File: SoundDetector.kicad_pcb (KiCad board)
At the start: 2 copper layers, 50.8 x 22.9 mm, 6 parts, among them J1 feather long, J2 feather short

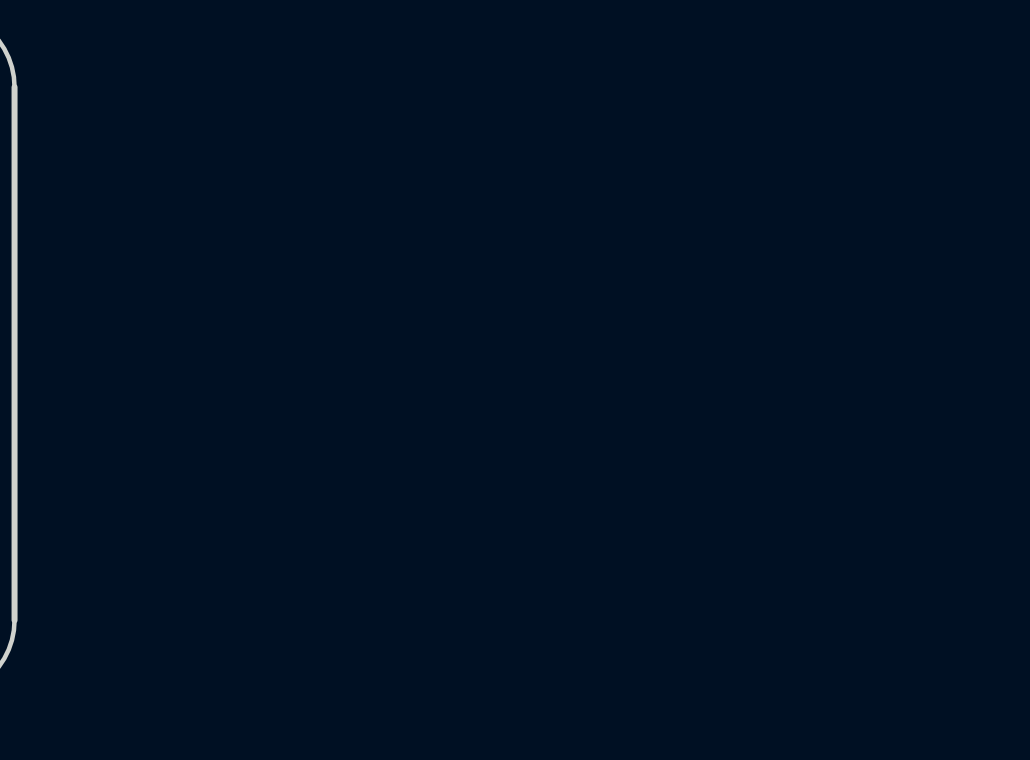
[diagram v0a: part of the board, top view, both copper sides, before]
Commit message: Import new footprints into PCB.
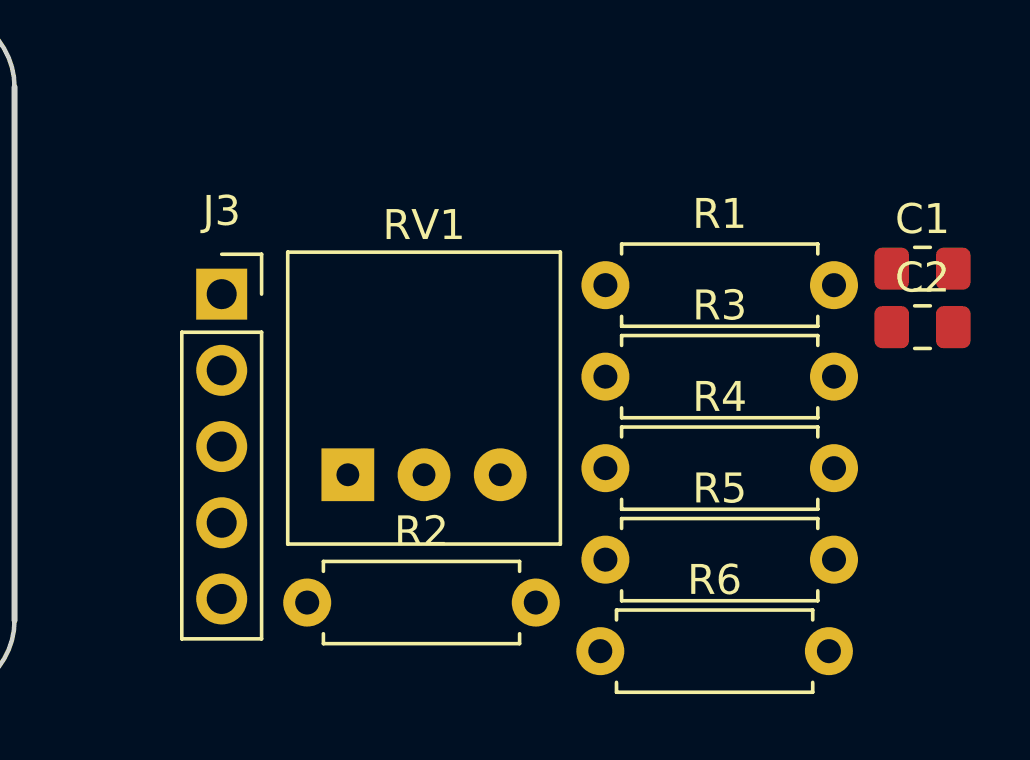
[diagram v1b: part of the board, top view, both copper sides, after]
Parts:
- added C1: 10μF, Capacitor_SMD:C_0805_2012Metric_Pad1.15x1.40mm_HandSolder, F.Cu at (106.5, 34.0)
- added C2: 10μF, Capacitor_SMD:C_0805_2012Metric_Pad1.15x1.40mm_HandSolder, F.Cu at (106.5, 35.9)
- added J3: sound detector, Connector_PinSocket_2.54mm:PinSocket_1x05_P2.54mm_Vertical, F.Cu at (83.1, 34.8)
- added R1: 1.74K, Resistor_THT:R_Axial_DIN0207_L6.3mm_D2.5mm_P7.62mm_Horizontal, F.Cu at (95.9, 34.5)
- added R2: 3.3K, Resistor_THT:R_Axial_DIN0207_L6.3mm_D2.5mm_P7.62mm_Horizontal, F.Cu at (86.0, 45.1)
- added R3: 1.74K, Resistor_THT:R_Axial_DIN0207_L6.3mm_D2.5mm_P7.62mm_Horizontal, F.Cu at (95.9, 37.6)
- added R4: 3.3K, Resistor_THT:R_Axial_DIN0207_L6.3mm_D2.5mm_P7.62mm_Horizontal, F.Cu at (95.9, 40.6)
- added R5: 1.74K, Resistor_THT:R_Axial_DIN0207_L6.3mm_D2.5mm_P7.62mm_Horizontal, F.Cu at (95.9, 43.7)
- added R6: 3.3K, Resistor_THT:R_Axial_DIN0207_L6.3mm_D2.5mm_P7.62mm_Horizontal, F.Cu at (95.7, 46.7)
- added RV1: 10K, footprints:Potentiometer_Bourns_3352T_Vertical, F.Cu at (87.3, 40.9)

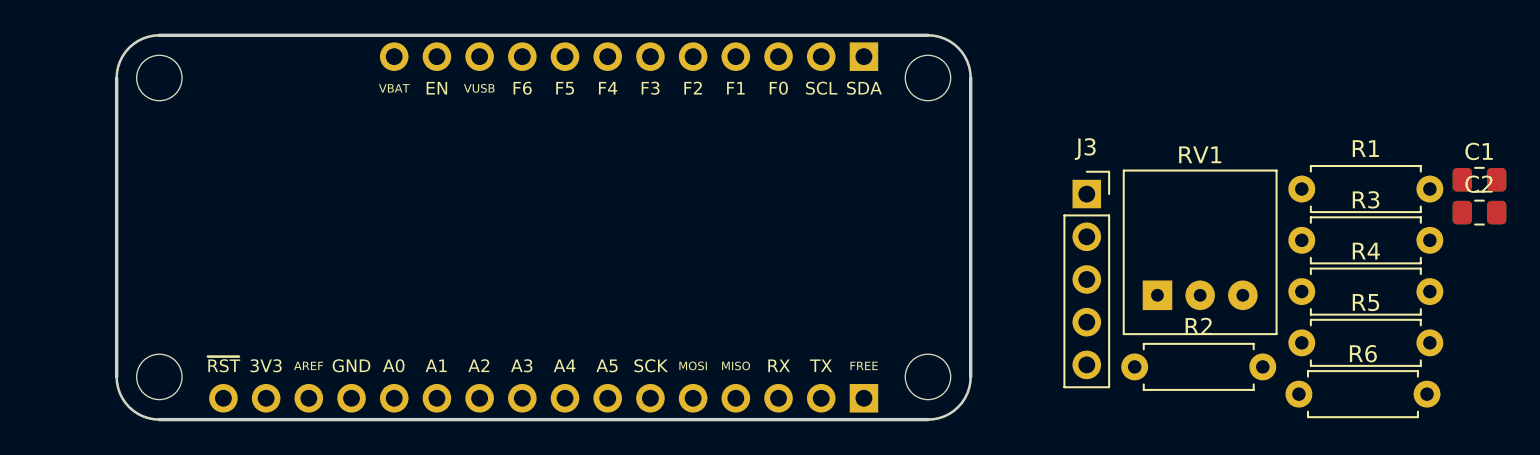
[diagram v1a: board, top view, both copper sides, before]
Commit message: Position footprints on PCB.
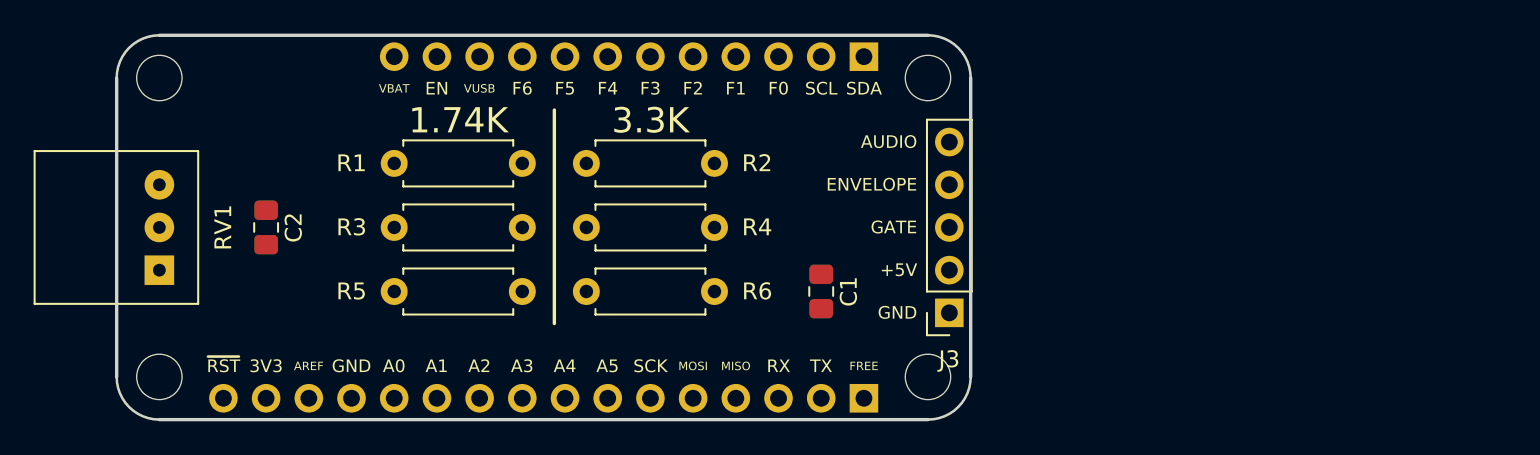
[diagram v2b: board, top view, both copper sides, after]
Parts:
- moved C2 72.2 mm to (34.3, 36.8), turned to 270 degrees
- moved RV1 59.4 mm to (27.9, 39.4), turned to 90 degrees
- moved R5 54.1 mm to (41.9, 40.6)
- moved R1 54.0 mm to (41.9, 33.0)
- moved R3 54.0 mm to (41.9, 36.8)
- moved R6 42.8 mm to (53.3, 40.6)
- moved R4 42.7 mm to (53.3, 36.8)
- moved C1 39.7 mm to (67.3, 40.6), turned to 270 degrees
- moved R2 34.8 mm to (53.3, 33.0)
- moved J3 10.8 mm to (74.9, 41.9), turned to 180 degrees
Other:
- board text added: "+5V"
- board text added: "1.74K"
- board text added: "3.3K"
- board text added: "AUDIO"
- board text added: "ENVELOPE"
- board text added: "GATE"

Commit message: Draw all the tracks.
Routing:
- net /VUSB: track 0.00 -> 41.2 mm, vias 0 -> 1
- net /GATE: track 0.00 -> 34.6 mm
- net /ENV: track 0.00 -> 34.1 mm
- net /AUD: track 0.00 -> 33.5 mm
- net /A2: track 0.00 -> 31.4 mm, vias 0 -> 1
- net /F0: track 0.00 -> 31.0 mm, vias 0 -> 1
- net /A0: track 0.00 -> 23.9 mm, vias 0 -> 1
- net +3V3: track 0.00 -> 21.2 mm, vias 0 -> 1
- net /A1: track 0.00 -> 19.1 mm, vias 0 -> 1
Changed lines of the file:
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@@
     (thickness 1.6)
     (drawings 44)
-    (tracks 0)
+    (tracks 48)
     (zones 0)
     (modules 16)
@@
   (setup
     (last_trace_width 0.25)
+    (user_trace_width 0.508)
     (trace_clearance 0.2)
     (zone_clearance 0.508)
@@
   (gr_line (start 76.2 27.94) (end 76.2 45.72) (layer Edge.Cuts) (width 0.2))
   (gr_line (start 27.94 25.4) (end 73.66 25.4) (layer Edge.Cuts) (width 0.2))
+  (segment (start 43.724999 36.680003) (end 43.724999 36.285001) (width 0.25) (layer F.Cu) (net 10))
+  (segment (start 27.94 36.83) (end 34.85319 36.83) (width 0.25) (layer F.Cu) (net 10))
+  (segment (start 34.85319 36.83) (end 35.978191 37.955001) (width 0.25) (layer F.Cu) (net 10))
+  (segment (start 35.978191 37.955001) (end 42.450001 37.955001) (width 0.25) (layer F.Cu) (net 10))
+  (segment (start 42.450001 37.955001) (end 43.724999 36.680003) (width 0.25) (layer F.Cu) (net 10))
+  (via (at 45.72 35.56) (size 0.8) (drill 0.4) (layers F.Cu B.Cu) (net 10))
+  (segment (start 44.45 35.56) (end 45.72 35.56) (width 0.25) (layer F.Cu) (net 10))
+  (segment (start 43.724999 36.285001) (end 44.45 35.56) (width 0.25) (layer F.Cu) (net 10))
+  (segment (start 45.72 45.72) (end 46.99 46.99) (width 0.25) (layer B.Cu) (net 10))
+  (segment (start 45.72 35.56) (end 45.72 45.72) (width 0.25) (layer B.Cu) (net 10))
+  (segment (start 49.53 36.83) (end 53.34 36.83) (width 0.25) (layer F.Cu) (net 11))
+  (via (at 44.45 36.83) (size 0.8) (drill 0.4) (layers F.Cu B.Cu) (net 11))
+  (segment (start 49.53 36.83) (end 44.45 36.83) (width 0.25) (layer F.Cu) (net 11))
+  (segment (start 44.45 36.83) (end 44.45 46.99) (width 0.25) (layer B.Cu) (net 11))
+  (segment (start 49.53 33.02) (end 53.34 33.02) (width 0.25) (layer F.Cu) (net 12))
+  (via (at 44.45 33.02) (size 0.8) (drill 0.4) (layers F.Cu B.Cu) (net 12))
+  (segment (start 49.53 33.02) (end 44.45 33.02) (width 0.25) (layer F.Cu) (net 12))
+  (segment (start 42.759999 46.140001) (end 41.91 46.99) (width 0.25) (layer B.Cu) (net 12))
+  (segment (start 43.18 45.72) (end 42.759999 46.140001) (width 0.25) (layer B.Cu) (net 12))
+  (segment (start 43.18 34.29) (end 43.18 45.72) (width 0.25) (layer B.Cu) (net 12))
+  (segment (start 44.45 33.02) (end 43.18 34.29) (width 0.25) (layer B.Cu) (net 12))
+  (segment (start 32.775 34.29) (end 34.29 35.805) (width 0.508) (layer F.Cu) (net 15))
+  (segment (start 27.94 34.29) (end 32.775 34.29) (width 0.508) (layer F.Cu) (net 15))
+  (via (at 36.83 36.83) (size 0.8) (drill 0.4) (layers F.Cu B.Cu) (net 15))
+  (segment (start 35.805 35.805) (end 36.83 36.83) (width 0.508) (layer F.Cu) (net 15))
+  (segment (start 34.29 35.805) (end 35.805 35.805) (width 0.508) (layer F.Cu) (net 15))
+  (segment (start 34.29 39.37) (end 34.29 46.99) (width 0.508) (layer B.Cu) (net 15))
+  (segment (start 36.83 36.83) (end 34.29 39.37) (width 0.508) (layer B.Cu) (net 15))
+  (segment (start 49.53 40.64) (end 53.34 40.64) (width 0.25) (layer F.Cu) (net 19))
+  (via (at 64.77 41.91) (size 0.8) (drill 0.4) (layers F.Cu B.Cu) (net 19))
+  (segment (start 54.61 41.91) (end 64.77 41.91) (width 0.25) (layer F.Cu) (net 19))
+  (segment (start 53.34 40.64) (end 54.61 41.91) (width 0.25) (layer F.Cu) (net 19))
+  (segment (start 64.77 41.91) (end 64.77 26.67) (width 0.25) (layer B.Cu) (net 19))
+  (segment (start 67.555 39.37) (end 67.31 39.615) (width 0.508) (layer F.Cu) (net 26))
+  (segment (start 74.93 39.37) (end 67.555 39.37) (width 0.508) (layer F.Cu) (net 26))
+  (via (at 46.99 39.37) (size 0.8) (drill 0.4) (layers F.Cu B.Cu) (net 26))
+  (segment (start 47.368372 38.991628) (end 46.99 39.37) (width 0.508) (layer F.Cu) (net 26))
+  (segment (start 66.686628 38.991628) (end 47.368372 38.991628) (width 0.508) (layer F.Cu) (net 26))
+  (segment (start 67.31 39.615) (end 66.686628 38.991628) (width 0.508) (layer F.Cu) (net 26))
+  (segment (start 46.99 39.37) (end 46.99 26.67) (width 0.508) (layer B.Cu) (net 26))
+  (segment (start 44.594999 37.955001) (end 42.709999 39.840001) (width 0.25) (layer F.Cu) (net 29))
+  (segment (start 73.804999 37.955001) (end 44.594999 37.955001) (width 0.25) (layer F.Cu) (net 29))
+  (segment (start 42.709999 39.840001) (end 41.91 40.64) (width 0.25) (layer F.Cu) (net 29))
+  (segment (start 74.93 36.83) (end 73.804999 37.955001) (width 0.25) (layer F.Cu) (net 29))
+  (segment (start 44.45 34.29) (end 41.91 36.83) (width 0.25) (layer F.Cu) (net 30))
+  (segment (start 74.93 34.29) (end 44.45 34.29) (width 0.25) (layer F.Cu) (net 30))
+  (segment (start 43.18 31.75) (end 41.91 33.02) (width 0.25) (layer F.Cu) (net 31))
+  (segment (start 74.93 31.75) (end 43.18 31.75) (width 0.25) (layer F.Cu) (net 31))
 )

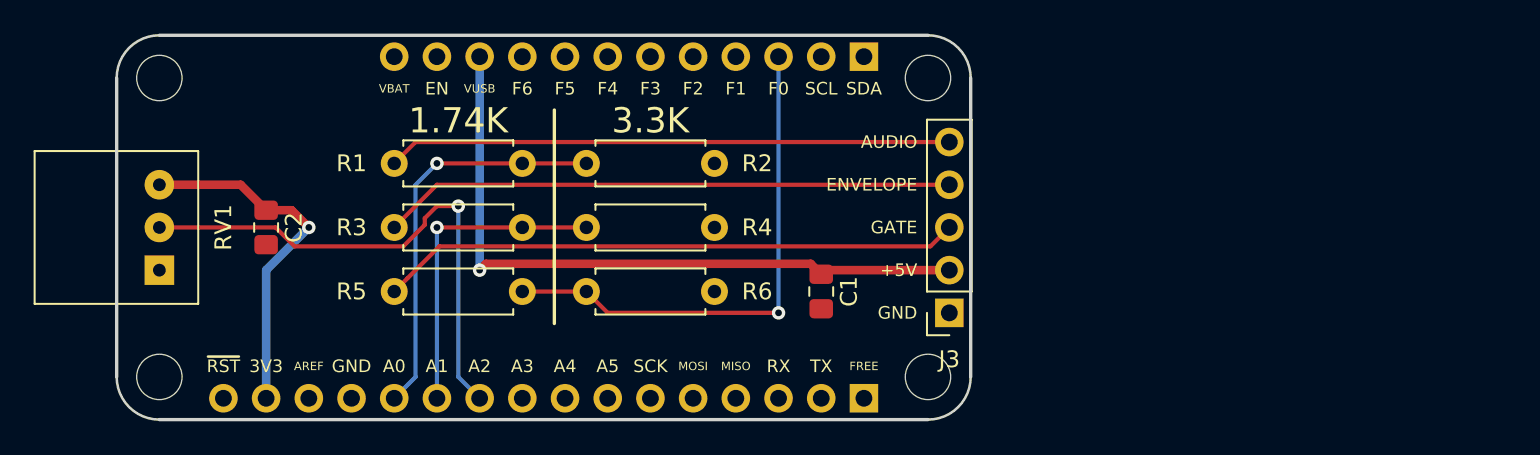
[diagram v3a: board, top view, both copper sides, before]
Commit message: Fill GND zones.
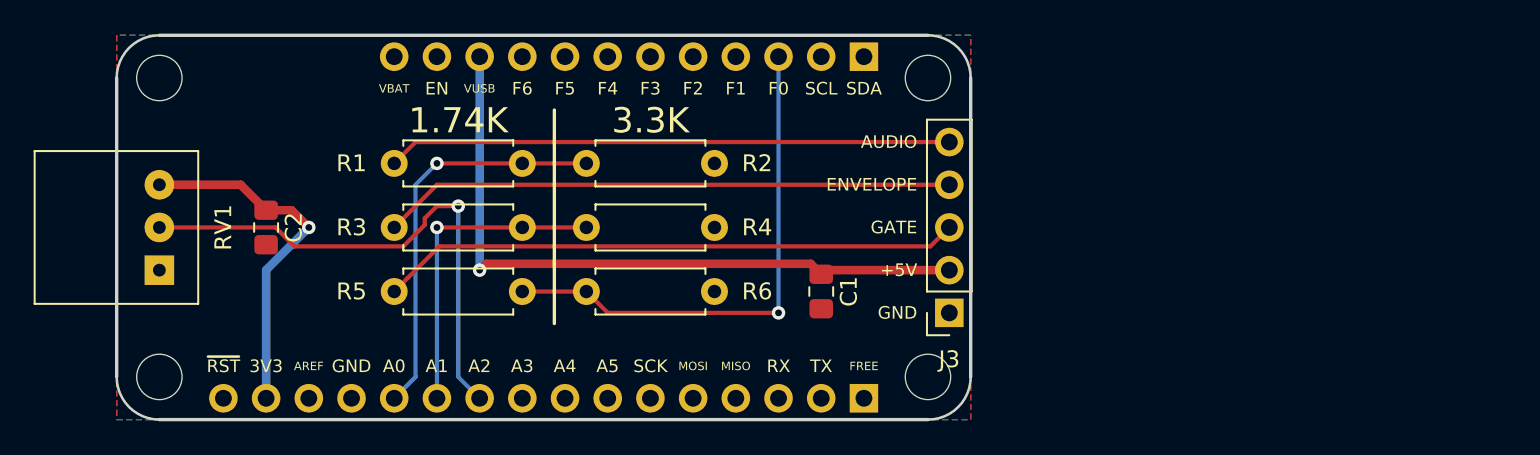
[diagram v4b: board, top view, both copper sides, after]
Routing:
- added copper zone on B.Cu, net GND
- added copper zone on F.Cu, net GND
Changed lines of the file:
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@@
   (segment (start 43.18 31.75) (end 41.91 33.02) (width 0.25) (layer F.Cu) (net 31))
   (segment (start 74.93 31.75) (end 43.18 31.75) (width 0.25) (layer F.Cu) (net 31))
+  (zone (net 13) (net_name GND) (layer B.Cu) (hatch edge 0.508)
+    (connect_pads (clearance 0.508))
+    (min_thickness 0.254)
+    (fill yes (arc_segments 16) (thermal_gap 0.508) (thermal_bridge_width 0.508))
+    (polygon
+      (pts
+        (xy 25.4 25.4) (xy 25.4 48.26) (xy 76.2 48.26) (xy 76.2 25.4)
+      )
+    )
+  )
+  (zone (net 13) (net_name GND) (layer F.Cu) (hatch edge 0.508)
+    (connect_pads (clearance 0.508))
+    (min_thickness 0.254)
+    (fill yes (arc_segments 16) (thermal_gap 0.508) (thermal_bridge_width 0.508))
+    (polygon
+      (pts
+        (xy 25.4 25.4) (xy 25.4 48.26) (xy 76.2 48.26) (xy 76.2 25.4)
+      )
+    )
+  )
 )

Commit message: Add information on back silkscreen.
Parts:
- added REF**: OSHW-Symbol_6.7x6mm_SilkScreen, Symbol:OSHW-Symbol_6.7x6mm_SilkScreen, B.Cu at (68.6, 36.8)
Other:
- board text added: "2019-07-24"
- board text added: "CC-BY-SA 4.0"
- board text added: "Patrick Pelletier"
- board text added: "Sound Detector FeatherWing 1.0"

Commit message: Put GitHub URL on silkscreen.
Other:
- board text added: "https://github.com/ppelleti/SoundDetectorWing"
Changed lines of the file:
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@@
   (general
     (thickness 1.6)
-    (drawings 48)
+    (drawings 49)
     (tracks 48)
     (zones 0)
@@
     (descr "Through hole straight pin header, 1x16, 2.54mm pitch, single row")
     (tags "Through hole pin header THT 1x16 2.54mm single row")
-    (fp_text reference J1 (at 0 2.33 90) (layer B.SilkS) hide
+    (fp_text reference J1 (at 2.54 -30.48 180) (layer B.SilkS)
       (effects (font (size 1 1) (thickness 0.15)) (justify mirror))
     )
@@
     (descr "Through hole straight pin header, 1x12, 2.54mm pitch, single row")
     (tags "Through hole pin header THT 1x12 2.54mm single row")
-    (fp_text reference J2 (at 0 2.33 90) (layer B.SilkS) hide
+    (fp_text reference J2 (at 0 -30.48 90) (layer B.SilkS)
       (effects (font (size 1 1) (thickness 0.15)) (justify mirror))
     )
@@
     (descr "Through hole straight socket strip, 1x05, 2.54mm pitch, single row (from Kicad 4.0.7), script generated")
     (tags "Through hole socket strip THT 1x05 2.54mm single row")
-    (fp_text reference J3 (at 0 -2.77 180) (layer F.SilkS)
+    (fp_text reference J3 (at 2.54 -1.905 180) (layer F.SilkS)
       (effects (font (size 1 1) (thickness 0.15)))
     )
@@
       (xy 0.555814 2.531069)) (layer B.SilkS) (width 0.01))
   )
+  (gr_text https://github.com/ppelleti/SoundDetectorWing (at 51.435 34.925) (layer B.SilkS)
+    (effects (font (size 0.75 0.75) (thickness 0.15)) (justify mirror))
+  )
   (gr_text "CC-BY-SA\n4.0" (at 68.58 41.91) (layer B.SilkS)
